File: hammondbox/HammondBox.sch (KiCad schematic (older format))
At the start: 14 parts, among them P1 USB_OTG, P2 CONN_02X03, P3 CONN_01X08, U1 ESP-12E, U2 TLV70233DBV

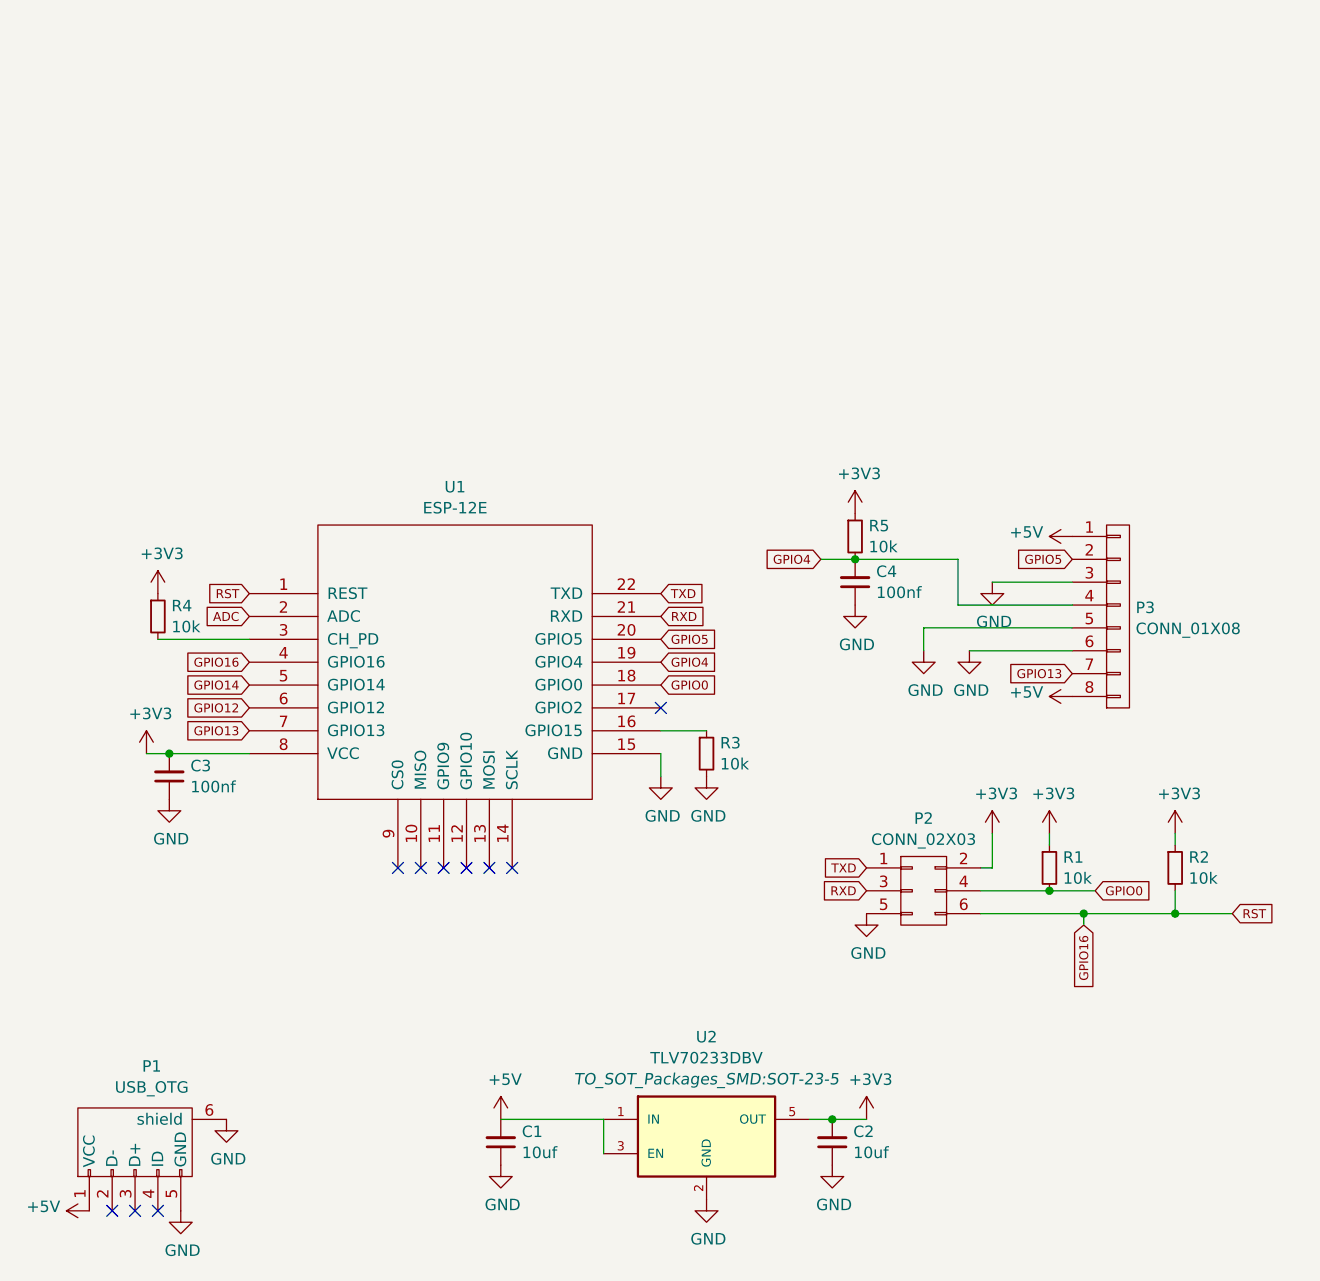
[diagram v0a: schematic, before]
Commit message: Use MCP1702 for regulator, use reflow sized pads.
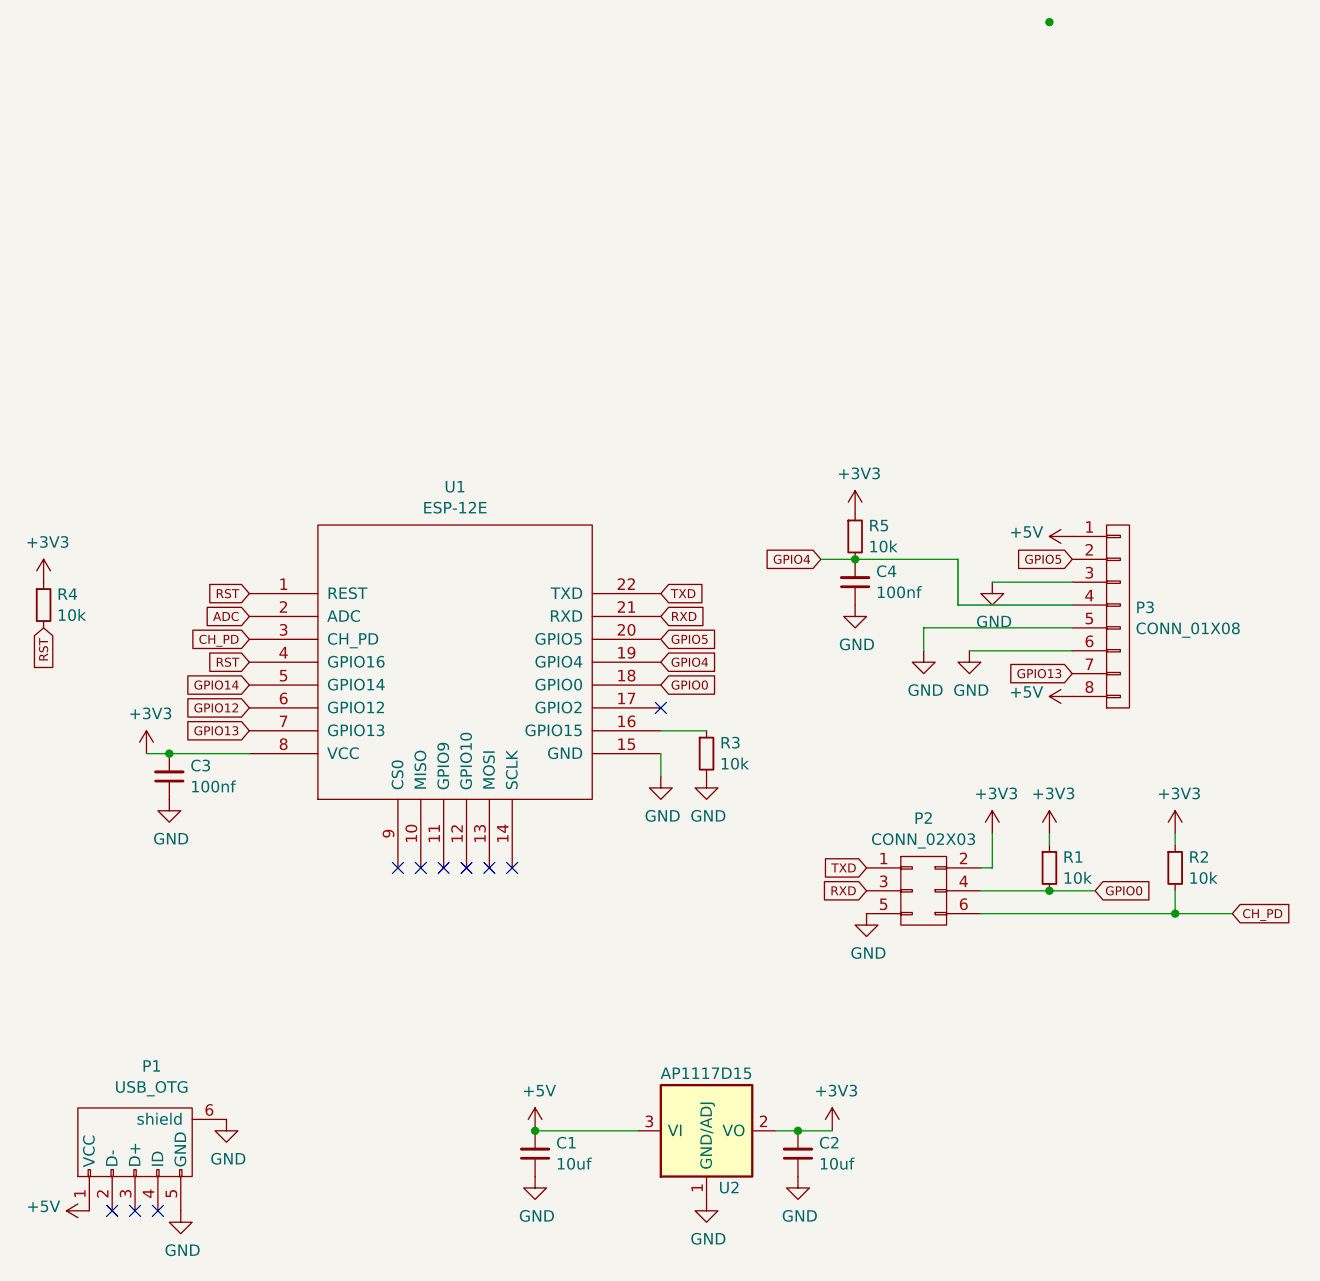
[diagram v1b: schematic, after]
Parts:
- removed U2: TLV70233DBV, TO_SOT_Packages_SMD:SOT-23-5, symbol TLV70233DBV
- added U2: AP1117D15, TO_SOT_Packages_SMD:SOT-23, symbol AP1117D15
- C1, C2: footprint Capacitors_SMD:C_0805_HandSoldering -> Capacitors_SMD:C_0805
- C3, C4: footprint Capacitors_SMD:C_0603_HandSoldering -> Capacitors_SMD:C_0603
- R1, R2, R3, R4, R5: footprint Resistors_SMD:R_0603_HandSoldering -> Resistors_SMD:R_0603
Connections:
- net +3V3: now also U2.2 (VO)
- net +5V: now also U2.3 (VI)
- net GND: now also U2.1 (GND/ADJ)
- net CH_PD: now reaches U1.3 (CH_PD)
- net CH_PD: now also P2.6 (P6), R2.2; no longer R4.2
- net GPIO16 renamed RST
- net RST: now also R4.2; no longer P2.6 (P6), R2.2
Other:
- moved on the sheet: C1, C2, R4
